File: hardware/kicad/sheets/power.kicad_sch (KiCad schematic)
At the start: 27 parts, among them J2 24V_IN, Q8 AO3401A, U11 XL1509-5.0E1, U12 TPS2116DRLR, U2 TLV1117LV33

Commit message: hardware: clear three of the four ERC errors on the power sheet
All three were power-flag bookkeeping, not wiring faults:

- #FLG02 put a PWR_FLAG on +5V, which U12's VOUT (a power output) already
  drives, so ERC saw two power outputs on one net. It is gone, with the
  +5V symbol and the three wire segments that only existed to hang it.
- BUCK_5V reaches U12's VIN1 only through L1, and VIN_P reaches U11's VIN
  only through Q8 - both passive - so ERC found no driver for either
  power input. Each gets a PWR_FLAG, laid out like the existing VIN flag
  (flag, 2.54 mm stub, vertical global label).

ERC: 234 items / 4 errors -> 230 / 1. The one left is U3/U5 SDO sharing
SPI_MISO: the MAX31856 tri-states SDO with CS high, but the library
symbol types the pin as a plain Output. Warnings drop by one because the
removed +5V symbol was a stale library copy. The netlist content is
unchanged (PWR_FLAGs are virtual), so the board is untouched.

Edited through Konnect, then re-saved with `kicad-cli sch upgrade --force`
so the sheet keeps KiCad's own formatting.

Co-Authored-By: Claude Opus 5.5 <noreply@anthropic.com>
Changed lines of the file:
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@@
 	(wire
 		(pts
-			(xy 22.86 247.65) (xy 22.86 250.19)
-		)
-		(stroke
-			(width 0)
-			(type default)
-		)
-	)
-	(wire
-		(pts
 			(xy 49.53 111.76) (xy 49.53 121.92)
 		)
@@
 	(wire
 		(pts
-			(xy 26.67 250.19) (xy 26.67 243.84)
-		)
-		(stroke
-			(width 0)
-			(type default)
-		)
-	)
-	(wire
-		(pts
 			(xy 24.13 171.45) (xy 50.8 171.45)
 		)
@@
 	(wire
 		(pts
-			(xy 22.86 250.19) (xy 26.67 250.19)
-		)
-		(stroke
-			(width 0)
-			(type default)
-		)
-	)
-	(wire
-		(pts
 			(xy 179.07 115.57) (xy 179.07 113.03)
 		)
@@
 	(wire
 		(pts
+			(xy 69.85 241.3) (xy 69.85 243.84)
+		)
+		(stroke
+			(width 0)
+			(type default)
+		)
+	)
+	(wire
+		(pts
 			(xy 212.09 80.01) (xy 214.63 80.01)
 		)
@@
 	(wire
 		(pts
+			(xy 85.09 241.3) (xy 85.09 243.84)
+		)
+		(stroke
+			(width 0)
+			(type default)
+		)
+	)
+	(wire
+		(pts
 			(xy 60.96 184.15) (xy 60.96 186.69)
 		)
@@
 	(global_label "VIN_P"
 		(shape passive)
+		(at 85.09 243.84 270)
+		(effects
+			(font
+				(size 1.27 1.27)
+			)
+			(justify right)
+		)
+		(property "Intersheetrefs" "${INTERSHEET_REFS}"
+			(at 85.09 243.84 0)
+			(hide yes)
+			(show_name no)
+			(do_not_autoplace no)
+			(effects
+				(font
+					(size 1.27 1.27)
+				)
+			)
+		)
+	)
+	(global_label "VIN_P"
+		(shape passive)
 		(at 161.29 80.01 180)
 		(effects
@@
 		)
 	)
+	(global_label "BUCK_5V"
+		(shape passive)
+		(at 69.85 243.84 270)
+		(effects
+			(font
+				(size 1.27 1.27)
+			)
+			(justify right)
+		)
+		(property "Intersheetrefs" "${INTERSHEET_REFS}"
+			(at 69.85 243.84 0)
+			(hide yes)
+			(show_name no)
+			(do_not_autoplace no)
+			(effects
+				(font
+					(size 1.27 1.27)
+				)
+			)
+		)
+	)
 	(global_label "VIN_P"
 		(shape passive)
@@
 	)
 	(symbol
+		(lib_id "power:PWR_FLAG")
+		(at 69.85 241.3 0)
+		(unit 1)
+		(body_style 1)
+		(exclude_from_sim no)
+		(in_bom yes)
+		(on_board yes)
+		(in_pos_files yes)
+		(dnp no)
+		(property "Reference" "#FLG05"
+			(at 69.85 239.395 0)
+			(hide yes)
+			(show_name no)
+			(do_not_autoplace no)
+			(effects
+				(font
+					(size 1.27 1.27)
+				)
+			)
+		)
+		(property "Value" "PWR_FLAG"
+			(at 69.85 237.49 0)
+			(show_name no)
+			(do_not_autoplace no)
+			(effects
+				(font
+					(size 1.27 1.27)
+				)
+			)
+		)
+		(property "Footprint" ""
+			(at 69.85 241.3 0)
+			(hide yes)
+			(show_name no)
+			(do_not_autoplace no)
+			(effects
+				(font
+					(size 1.27 1.27)
+				)
+			)
+		)
+		(property "Datasheet" ""
+			(at 69.85 241.3 0)
+			(hide yes)
+			(show_name no)
+			(do_not_autoplace no)
+			(effects
+				(font
+					(size 1.27 1.27)
+				)
+			)
+		)
+		(property "Description" "Special symbol for telling ERC where power comes from"
+			(at 69.85 241.3 0)
+			(hide yes)
+			(show_name no)
+			(do_not_autoplace no)
+			(effects
+				(font
+					(size 1.27 1.27)
+				)
+			)
+		)
+		(pin "1"
+		)
+		(instances
+			(project "bisque-controller"
+				(path "/f24e0cd2-71c5-510c-9d15-562ab64c4388/c3ce2838-e44f-5ef5-9340-801a744d4591"
+					(reference "#FLG05")
+					(unit 1)
+				)
+			)
+		)
+	)
+	(symbol
 		(lib_id "power:+5V")
 		(at 41.91 205.74 0)
@@
 	)
 	(symbol
-		(lib_id "power:+5V")
-		(at 26.67 243.84 0)
-		(unit 1)
-		(body_style 1)
-		(exclude_from_sim no)
-		(in_bom yes)
-		(on_board yes)
-		(in_pos_files yes)
-		(dnp no)
-		(property "Reference" "#PWR0034"
-			(at 26.67 243.84 0)
-			(hide yes)
-			(show_name no)
-			(do_not_autoplace no)
-			(effects
-				(font
-					(size 1.27 1.27)
-				)
-			)
-		)
-		(property "Value" "+5V"
-			(at 26.67 240.0205 0)
-			(show_name no)
-			(do_not_autoplace no)
-			(effects
-				(font
-					(size 1.27 1.27)
-				)
-			)
-		)
-		(property "Footprint" ""
-			(at 26.67 243.84 0)
-			(hide yes)
-			(show_name no)
-			(do_not_autoplace no)
-			(effects
-				(font
-					(size 1.27 1.27)
-				)
-			)
-		)
-		(property "Datasheet" ""
-			(at 26.67 243.84 0)
-			(hide yes)
-			(show_name no)
-			(do_not_autoplace no)
-			(effects
-				(font
-					(size 1.27 1.27)
-				)
-			)
-		)
-		(property "Description" ""
-			(at 26.67 243.84 0)
-			(show_name no)
-			(do_not_autoplace no)
-			(effects
-				(font
-					(size 1.27 1.27)
-				)
-			)
-		)
-		(pin "1"
-		)
-		(instances
-			(project "bisque-controller"
-				(path "/f24e0cd2-71c5-510c-9d15-562ab64c4388/c3ce2838-e44f-5ef5-9340-801a744d4591"
-					(reference "#PWR0034")
-					(unit 1)
-				)
-			)
-		)
-	)
-	(symbol
 		(lib_id "power:GND")
 		(at 69.85 80.01 0)
@@
 	)
 	(symbol
-		(lib_id "power:PWR_FLAG")
-		(at 22.86 247.65 0)
-		(unit 1)
-		(body_style 1)
-		(exclude_from_sim no)
-		(in_bom yes)
-		(on_board yes)
-		(in_pos_files yes)
-		(dnp no)
-		(property "Reference" "#FLG02"
-			(at 22.86 243.65 0)
-			(hide yes)
-			(show_name no)
-			(do_not_autoplace no)
-			(effects
-				(font
-					(size 1.27 1.27)
-				)
-			)
-		)
-		(property "Value" "PWR_FLAG"
-			(at 22.86 241.65 0)
-			(hide yes)
-			(show_name no)
-			(do_not_autoplace no)
-			(effects
-				(font
-					(size 1.27 1.27)
-				)
-			)
-		)
-		(property "Footprint" ""
-			(at 22.86 247.65 0)
-			(hide yes)
-			(show_name no)
-			(do_not_autoplace no)
-			(effects
-				(font
-					(size 1.27 1.27)
-				)
-			)
-		)
-		(property "Datasheet" "~"
-			(at 22.86 247.65 0)
-			(hide yes)
-			(show_name no)
-			(do_not_autoplace no)
-			(effects
-				(font
-					(size 1.27 1.27)
-				)
-			)
-		)
-		(property "Description" ""
-			(at 22.86 247.65 0)
-			(show_name no)
-			(do_not_autoplace no)
-			(effects
-				(font
-					(size 1.27 1.27)
-				)
-			)
-		)
-		(pin "1"
-		)
-		(instances
-			(project "bisque-controller"
-				(path "/f24e0cd2-71c5-510c-9d15-562ab64c4388/c3ce2838-e44f-5ef5-9340-801a744d4591"
-					(reference "#FLG02")
-					(unit 1)
-				)
-			)
-		)
-	)
-	(symbol
 		(lib_id "Device:C")
 		(at 149.86 116.84 0)
@@
 					(unit 1)
 				)
+			)
+		)
+	)
+	(symbol
+		(lib_id "power:PWR_FLAG")
+		(at 85.09 241.3 0)
+		(unit 1)
+		(body_style 1)
+		(exclude_from_sim no)
+		(in_bom yes)
+		(on_board yes)
+		(in_pos_files yes)
+		(dnp no)
+		(property "Reference" "#FLG06"
+			(at 85.09 239.395 0)
+			(hide yes)
+			(show_name no)
+			(do_not_autoplace no)
+			(effects
+				(font
+					(size 1.27 1.27)
+				)
+			)
+		)
+		(property "Value" "PWR_FLAG"
+			(at 85.09 237.49 0)
+			(show_name no)
+			(do_not_autoplace no)
+			(effects
+				(font
+					(size 1.27 1.27)
+				)
+			)
+		)
+		(property "Footprint" ""
+			(at 85.09 241.3 0)
+			(hide yes)
+			(show_name no)
+			(do_not_autoplace no)
+			(effects
+				(font
+					(size 1.27 1.27)
+				)
+			)
+		)
+		(property "Datasheet" ""
+			(at 85.09 241.3 0)
+			(hide yes)
+			(show_name no)
+			(do_not_autoplace no)
+			(effects
+				(font
+					(size 1.27 1.27)
+				)
+			)
+		)
+		(property "Description" "Special symbol for telling ERC where power comes from"
+			(at 85.09 241.3 0)
+			(hide yes)
+			(show_name no)
+			(do_not_autoplace no)
+			(effects
+				(font
+					(size 1.27 1.27)
+				)
+			)
+		)
+		(pin "1"
+		)
+		(instances
+			(project "bisque-controller"
+				(path "/f24e0cd2-71c5-510c-9d15-562ab64c4388/c3ce2838-e44f-5ef5-9340-801a744d4591"
+					(reference "#FLG06")
+					(unit 1)
+				)

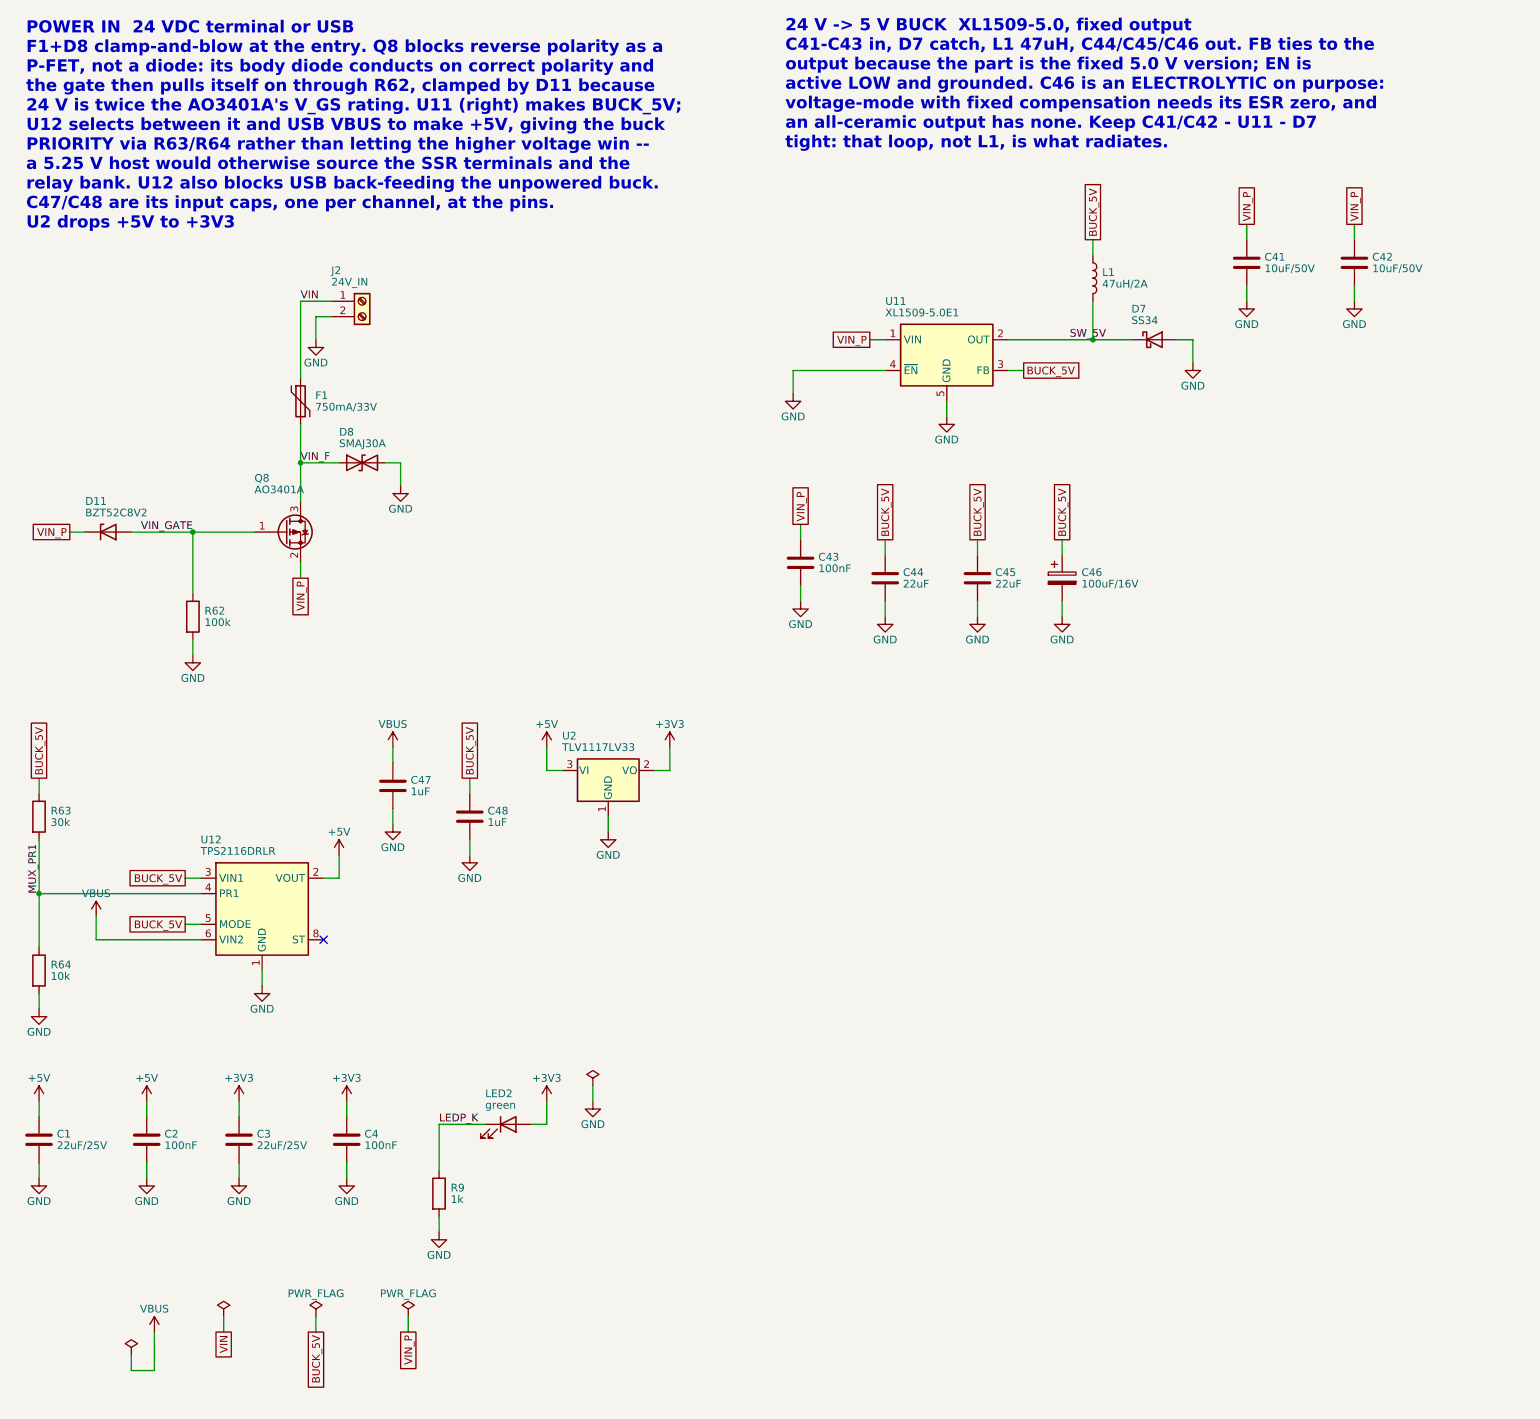
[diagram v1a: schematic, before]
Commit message: hardware: hierarchical schematic, ERC at 0/0, rev B.3
Applies items 1-3 of SCHEMATIC-REVIEW-2026-10-22.md.

ERC: the 173 lib_symbol_mismatch warnings were over-escaped quotes in the
embedded power symbols' Description strings; refreshed from the library.
The 18 off-grid power symbols are snapped and their stub wires redrawn.
The VIN and VLED global labels that existed only to carry a PWR_FLAG are
gone; the flags now sit on the nets they drive (J2.1, the VLED junction).
ERC reads 0 errors / 0 warnings with the documented SDO exclusion.

Hierarchy: no global labels remain. Each net that crosses sheets has one
hierarchical label per sheet, matching sheet pins on the root, and the
root wires those pins as a block diagram. Every other former global label
is a local label. The eight signal test points (TP4-TP11) move from the
test sheet to the mcu and ct sheets beside their nets, so the test block
needs no pins. KiCad names the nets /mcu/SPI_MISO etc.; netlist.py strips
the path, so the board's net names and the routing tables are unchanged
(182 components, 538 pads, 0 mismatches). single_global_label is now a
warning. check_sync_idempotent's collision fixture used the bare
"SPI_MISO" name and is updated, with a loud failure if its victims vanish.

Drawing: rev B.3 dated 2026-10-22 on every sheet, ct on A3 like the rest,
the three overflowing titles shortened, and the notes no longer refer to
design.py or to crystal load caps that no longer exist.

Co-Authored-By: Claude Fable 5.1 <noreply@anthropic.com>
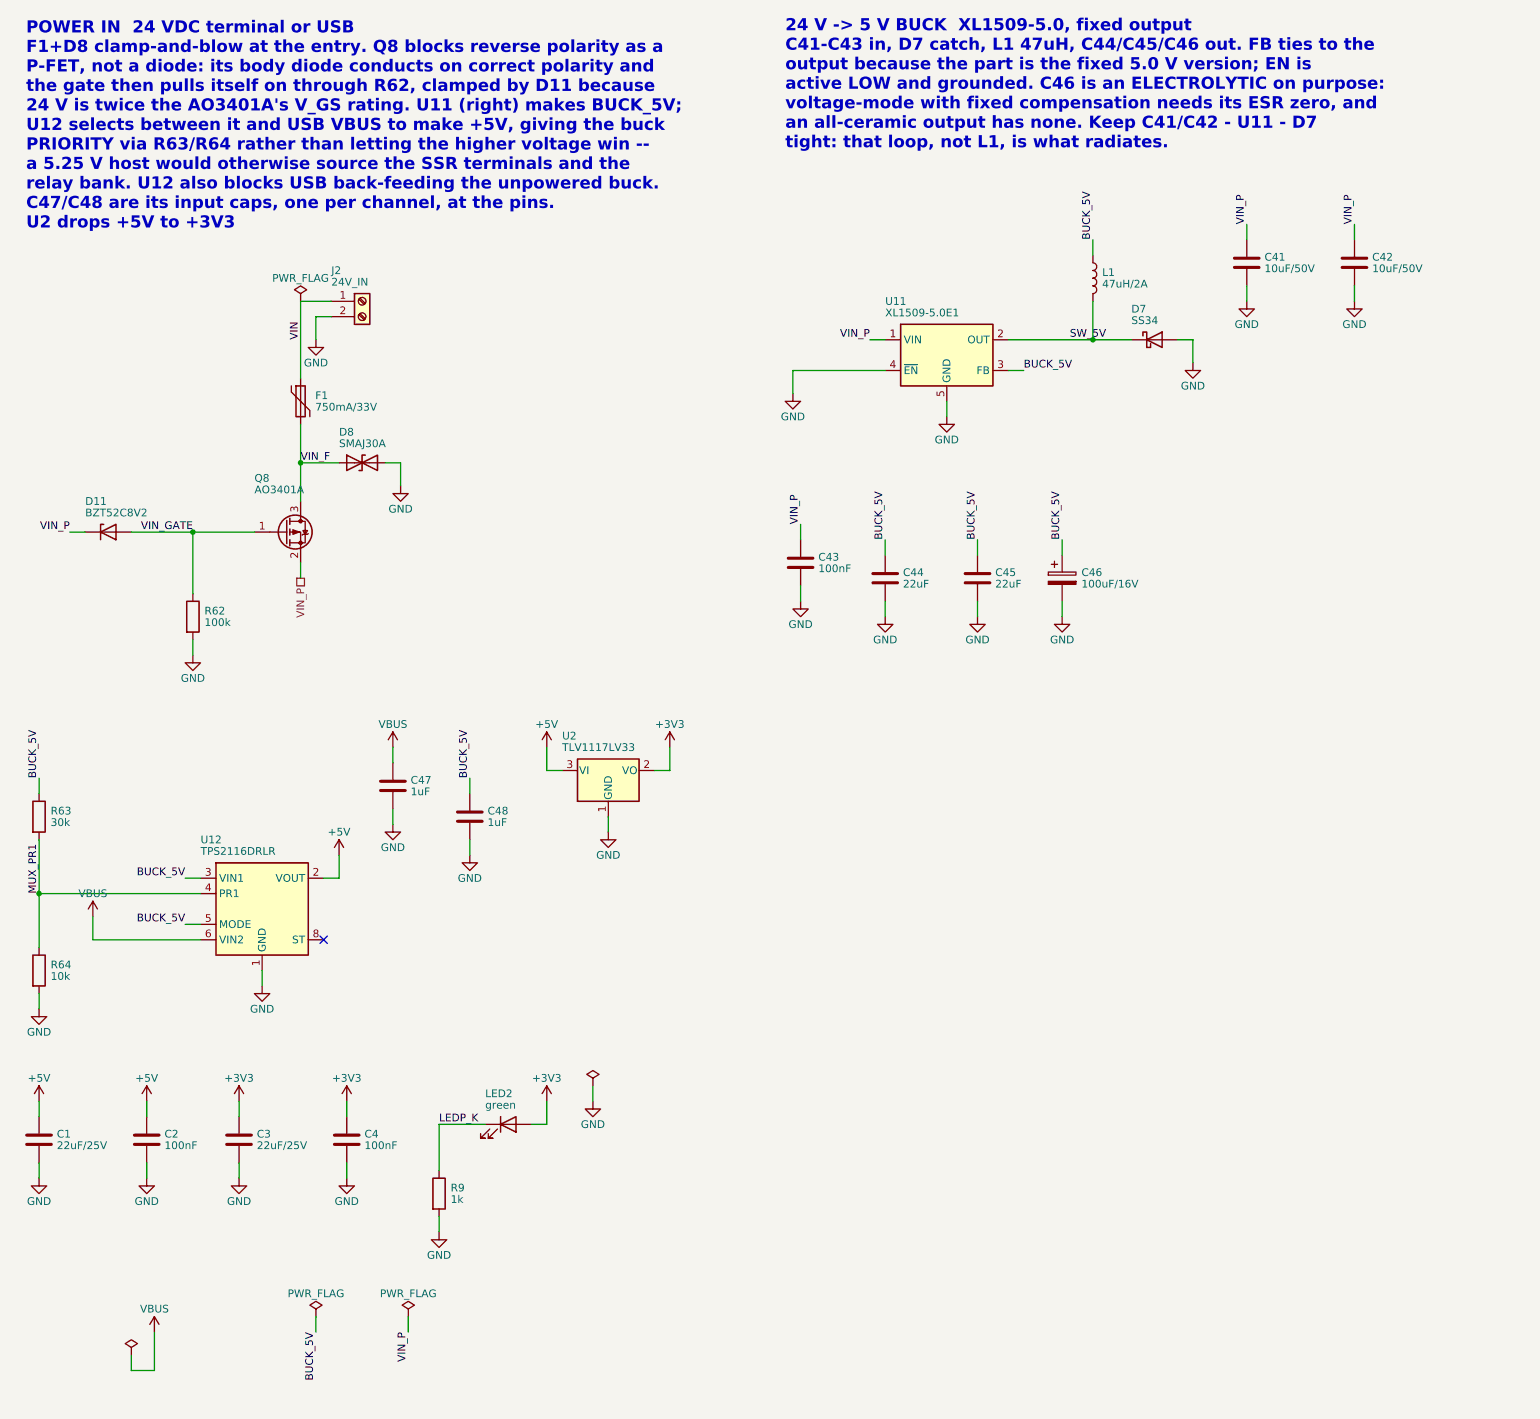
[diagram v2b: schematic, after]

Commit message: hardware: flags at their sources, tri-state MAX31856, Q4 flipped, make erc
Second batch from SCHEMATIC-REVIEW-2026-10-22.md (findings 5, 7, 14, 15,
16 and the local half of 19).

PWR_FLAGs: the power sheet's parked corner is gone. Each flag now sits
where its rail is created - J2.1 (VIN), J2.2 (GND), Q8 source (VIN_P),
L1 output (BUCK_5V) and J1 pin A4 (VBUS, on the mcu sheet) - with the
value text shown on all of them.

MAX31856: U3 and U5 now use bisque:MAX31856 from the new project library
bisque.kicad_sym (registered in sym-lib-table), a copy of the KiCad
symbol with SDO typed tri-state, which is what the part does while CS is
high. The ERC exclusion that papered over the shared SPI_MISO is removed;
ERC is clean with no exclusions.

Q4 is mirrored so the high-side P-FET reads source-up to +5V and drain
down to SSR_EN. One Value string per LCSC part (C38/C44/C45 22uF/25V,
R11 100R 1%); C46 moved 5 mm right to clear the longer text. Every test
point's Value is its net name (TP1 "+3V3" ... TP12 "WDT_CT_P"), so the
board's Value fields, the JLC BOM and the schematic PDF regenerate.

make erc runs kicad-cli ERC at every severity and fails on any
violation; lib_symbol_mismatch, endpoint_off_grid and
same_local_global_label are promoted to errors in the project. It is not
part of pcb-check or CI on purpose.

Board: sync changed only Value fields (0 re-netted); gerbers differ by
timestamp only; DRC 0; full make pcb-check passes.

Co-Authored-By: Claude Fable 5.1 <noreply@anthropic.com>
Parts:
- C44, C45: value 22uF -> 22uF/25V
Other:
- moved on the sheet: C46
